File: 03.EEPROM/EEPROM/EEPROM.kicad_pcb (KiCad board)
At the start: 2 copper layers, 0 parts

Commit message: EEPROM - PCB - ROUTING
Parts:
- added BT1: Battery, Connector_PinHeader_2.54mm:PinHeader_1x02_P2.54mm_Vertical, F.Cu at (75.5, 97.5)
- added C1: 0.1uF, Capacitor_SMD:C_0805_2012Metric, F.Cu at (92.3, 92.7)
- added C2: 22pF, Capacitor_SMD:C_0805_2012Metric, F.Cu at (108.0, 107.0)
- added C3: 22pF, Capacitor_SMD:C_0805_2012Metric, F.Cu at (96.3, 92.7)
- added C4: 0.1uF, Capacitor_SMD:C_0805_2012Metric, F.Cu at (108.3, 110.8)
- added C5: 100nF, Capacitor_SMD:C_0805_2012Metric, F.Cu at (100.3, 92.6)
- added D1: LED, LED_SMD:LED_0805_2012Metric_Pad1.15x1.40mm_HandSolder, F.Cu at (112.3, 93.0)
- added D2: LED, LED_SMD:LED_0805_2012Metric, F.Cu at (107.9, 92.8)
- added H1: MountingHole, MountingHole:MountingHole_2.1mm, F.Cu at (73.1, 90.0)
- added H2: MountingHole, MountingHole:MountingHole_2.1mm, F.Cu at (123.7, 90.0)
- added H3: MountingHole, MountingHole:MountingHole_2.1mm, F.Cu at (123.7, 120.3)
- added H4: MountingHole, MountingHole:MountingHole_2.1mm, F.Cu at (73.1, 120.3)
- added J1: Conn_01x04_Pin, Connector_PinHeader_2.54mm:PinHeader_1x04_P2.54mm_Vertical, F.Cu at (121.2, 106.0)
- added J2: Conn_01x09_Pin, Connector_PinHeader_2.54mm:PinHeader_1x09_P2.54mm_Vertical, F.Cu at (81.2, 117.8)
- added J3: Conn_01x04_Pin, Connector_PinHeader_2.54mm:PinHeader_1x04_P2.54mm_Vertical, F.Cu at (106.5, 117.8)
- added J4: Conn_02x03_Odd_Even, Connector_PinHeader_2.54mm:PinHeader_2x03_P2.54mm_Vertical, F.Cu at (119.0, 96.8)
- added R1: 10K, Resistor_SMD:R_0805_2012Metric, F.Cu at (81.3, 114.0)
- added R2: 10K, Resistor_SMD:R_0805_2012Metric, F.Cu at (85.7, 114.0)
- added R3: 4.7 K, Resistor_SMD:R_0805_2012Metric, F.Cu at (108.0, 99.9)
- added R4: 4.7 K, Resistor_SMD:R_0805_2012Metric, F.Cu at (108.0, 103.4)
- added R5: 330, Resistor_SMD:R_0805_2012Metric, F.Cu at (108.0, 96.5)
- added R6: 10 K, Resistor_SMD:R_0805_2012Metric, F.Cu at (112.1, 100.6)
- added R7: 330, Resistor_SMD:R_0805_2012Metric, F.Cu at (112.0, 97.1)
- added U1: 24LC1025, Package_SO:SOIC-8_5.3x5.3mm_P1.27mm, F.Cu at (84.1, 101.5)
- added U2: DS1337S_, LED_SMD:LED_0805_2012Metric_Pad1.15x1.40mm_HandSolder, F.Cu at (83.5, 108.5)
- added U3: 24LC1025, Package_SO:SOIC-8_5.3x5.3mm_P1.27mm, F.Cu at (84.1, 94.1)
- added U4: ATMEGA328P-AU, ATMEGA328P-AU:QFP80P900X900X120-32N, F.Cu at (96.0, 101.3)
- added Y1: 32.728 KHz, Crystal:Crystal_SMD_5032-2Pin_5.0x3.2mm_HandSoldering, F.Cu at (75.5, 108.5)
- added Y2: 16 MHz, Crystal:Crystal_SMD_5032-2Pin_5.0x3.2mm_HandSoldering, F.Cu at (95.9, 110.2)
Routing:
- net GND: track 0.00 -> 148.0 mm, vias 0 -> 3
- net /Vcc: track 0.00 -> 130.6 mm, vias 0 -> 2
- net /SCK: track 0.00 -> 87.5 mm, vias 0 -> 3
- net /SDA: track 0.00 -> 76.6 mm, vias 0 -> 3
- net Net-(BT1-+): track 0.00 -> 59.4 mm, vias 0 -> 2
- net /RESET: track 0.00 -> 33.3 mm, vias 0 -> 2
- net /TX: track 0.00 -> 31.7 mm, vias 0 -> 1
- net /MOSI: track 0.00 -> 29.5 mm
- net /D2: track 0.00 -> 28.0 mm, vias 0 -> 1
- net /RX: track 0.00 -> 27.8 mm, vias 0 -> 1
- net /MISO: track 0.00 -> 24.5 mm, vias 0 -> 1
- net Net-(U4-PB6): track 0.00 -> 24.5 mm
- net /D3: track 0.00 -> 23.9 mm, vias 0 -> 1
- net Net-(U4-PB7): track 0.00 -> 23.7 mm, vias 0 -> 3
- net /D4: track 0.00 -> 21.7 mm, vias 0 -> 1
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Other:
- board outline added: 55.7 x 35.3 mm
- board text added: "Gobal Krishnan V Practise 0.0.3"

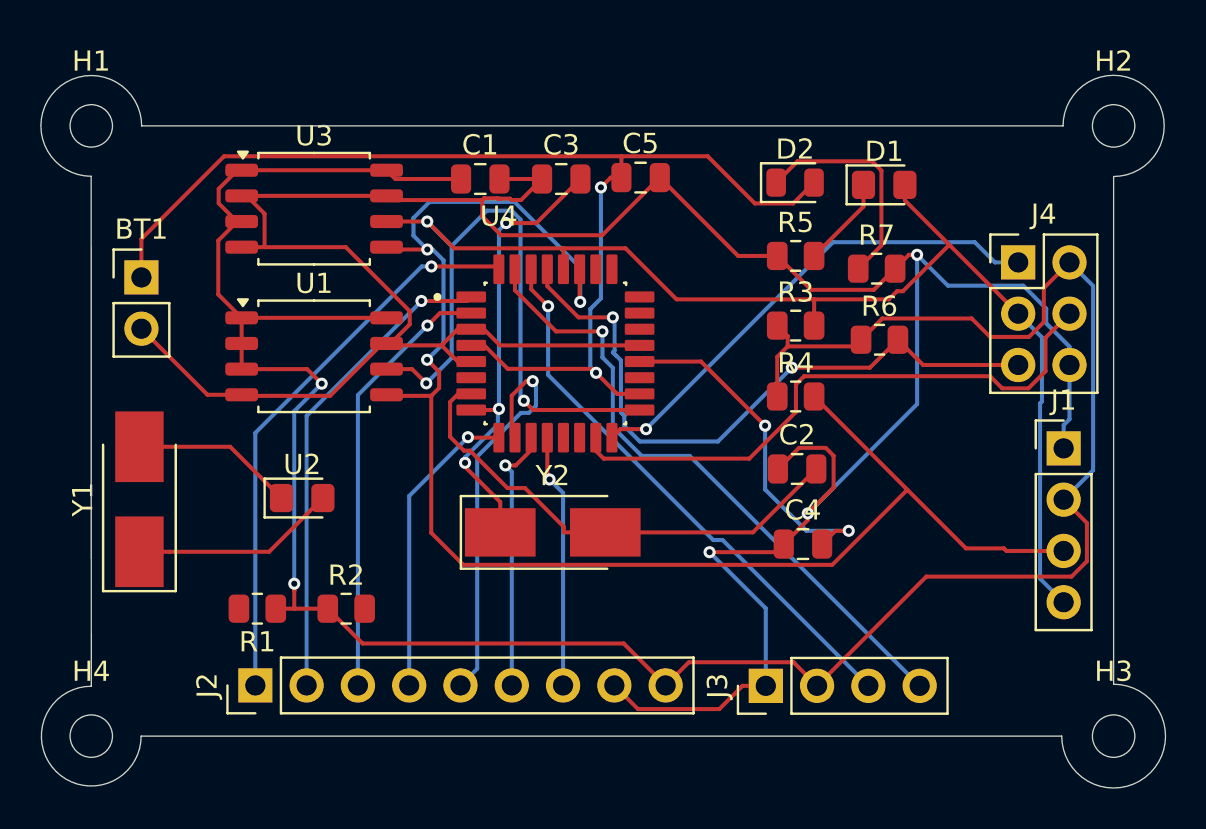
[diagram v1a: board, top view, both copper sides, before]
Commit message: EEPROM - PCB - LAYER 2 COPPER FILL
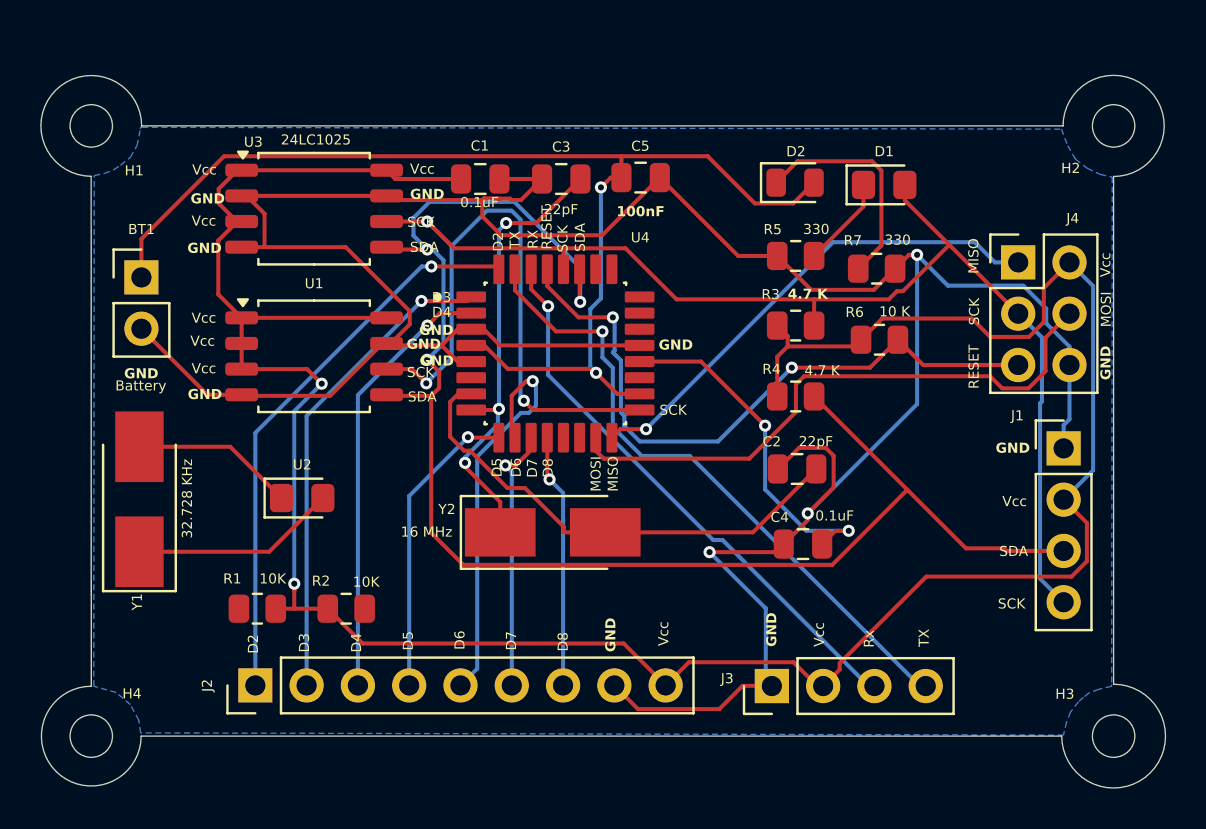
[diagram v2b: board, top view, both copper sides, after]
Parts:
- moved J3 0.30 mm to (106.8, 117.8)
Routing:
- added copper zone on B.Cu, net GND
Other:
- board text added: "D2"
- board text added: "D3"
- board text added: "D4"
- board text added: "D5"
- board text added: "D6"
- board text added: "D7"
- board text added: "D8"
- board text added: "GND"
- board text added: "MISO"
- board text added: "MOSI"
- board text added: "RESET"
- board text added: "RX"
- board text added: "Rx"
- board text added: "SCK"
- board text added: "SDA"
- board text added: "TX"
- board text added: "Vcc"
